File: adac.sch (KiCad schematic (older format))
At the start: 26 parts, among them J1 Conn_Coaxial, J2 Conn_Coaxial, J3 Conn_Coaxial, SW1 SW_SPST, U1 LTC1740, U2 TXS0108EPW, U3 TXS0108EPW, U4 AD7840

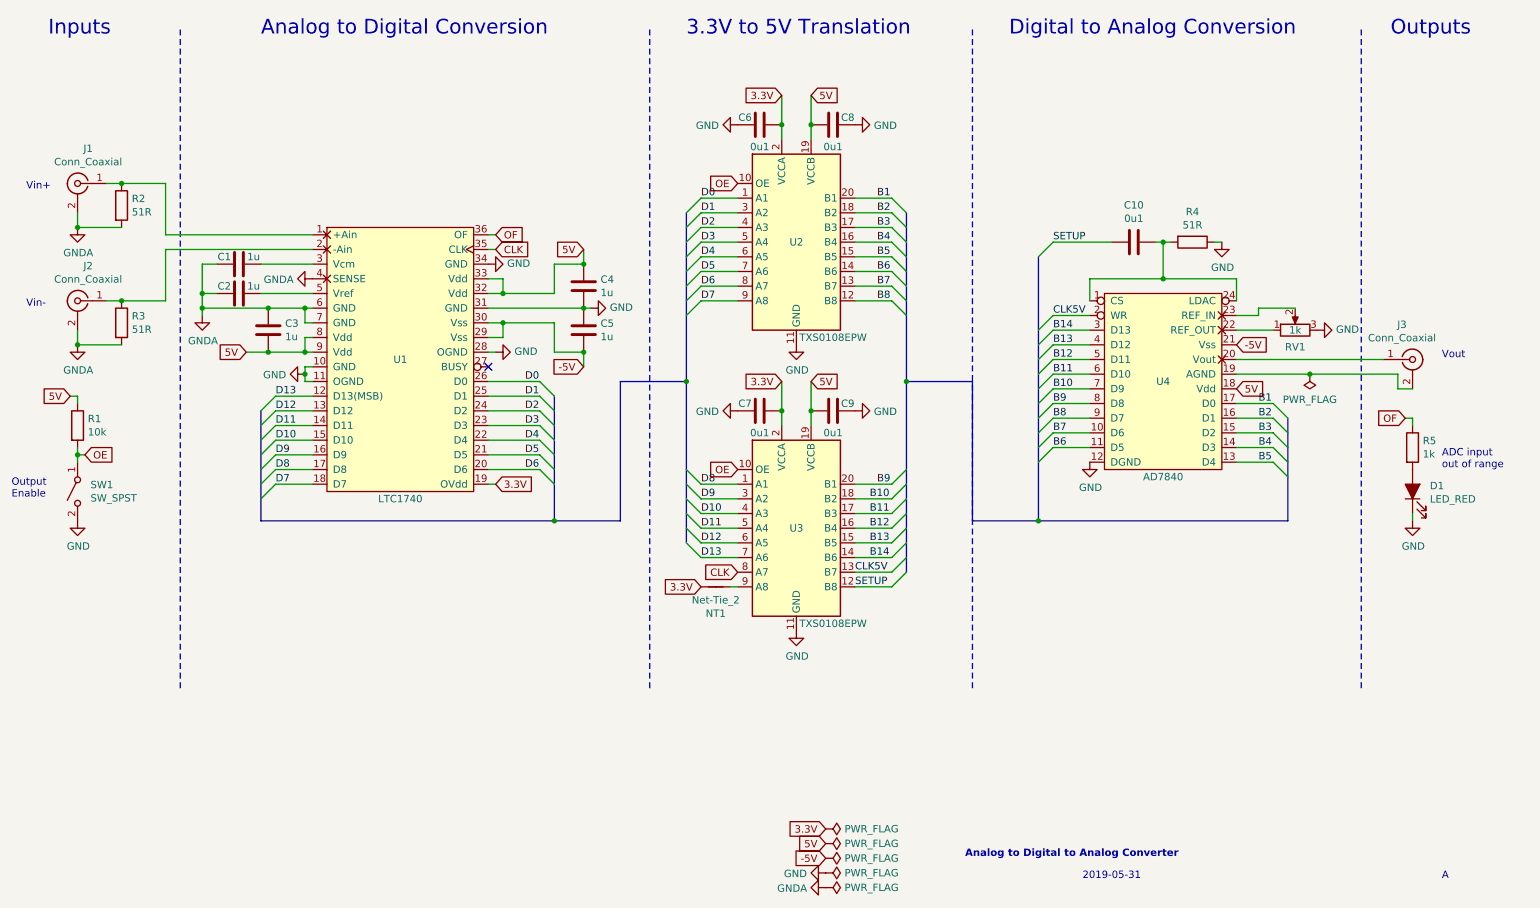
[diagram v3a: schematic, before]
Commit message: Add clock input connector
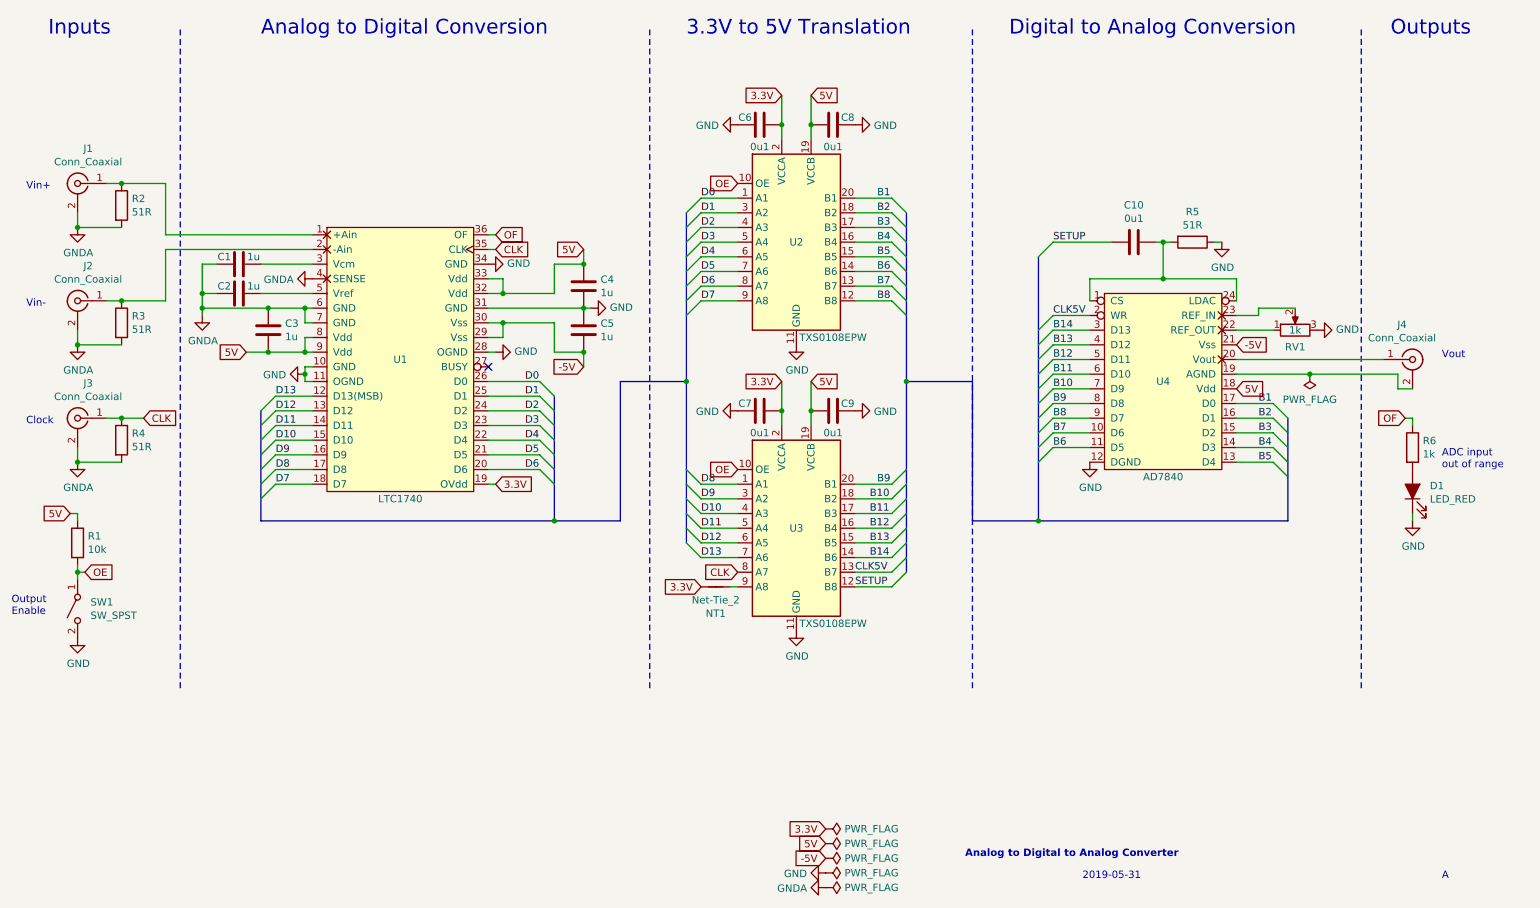
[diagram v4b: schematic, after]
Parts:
- added J3: Conn_Coaxial, Connector_Coaxial:BNC_TEConnectivity_1478204_Vertical, symbol Connector:Conn_Coaxial
- added R4: 51R, Resistor_THT:R_Axial_DIN0204_L3.6mm_D1.6mm_P7.62mm_Horizontal, symbol Device:R
- renumbered J3 to J4, R4 to R5, R5 to R6
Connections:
- net CLK: now also J3.1 (In), R4.1
- net GNDA: now also J3.2 (Ext), R4.2
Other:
- note added: "Clock"
- moved on the sheet: R1, SW1
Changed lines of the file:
@@
 	2850 4250 2850 4200
 $Comp
-L power:GND #PWR05
+L power:GND #PWR06
 U 1 1 5CF1A1D6
 P 2850 4200
-F 0 "#PWR05" H 2850 3950 50  0001 C CNN
+F 0 "#PWR06" H 2850 3950 50  0001 C CNN
 F 1 "GND" V 2855 4072 50  0000 R CNN
 F 2 "" H 2850 4200 50  0001 C CNN
@@
 	4150 3350 4100 3350
 $Comp
-L power:GND #PWR07
+L power:GND #PWR08
 U 1 1 5CF3FF9C
 P 4100 3450
-F 0 "#PWR07" H 4100 3200 50  0001 C CNN
+F 0 "#PWR08" H 4100 3200 50  0001 C CNN
 F 1 "GND" V 4105 3322 50  0000 R CNN
 F 2 "" H 4100 3450 50  0001 C CNN
@@
 Connection ~ 4200 3650
 $Comp
-L power:GND #PWR08
+L power:GND #PWR09
 U 1 1 5CF52655
 P 4150 4050
-F 0 "#PWR08" H 4150 3800 50  0001 C CNN
+F 0 "#PWR09" H 4150 3800 50  0001 C CNN
 F 1 "GND" V 4155 3922 50  0000 R CNN
 F 2 "" H 4150 4050 50  0001 C CNN
@@
 Connection ~ 4750 3450
 $Comp
-L power:GND #PWR012
+L power:GND #PWR013
 U 1 1 5CF89283
 P 6200 4000
-F 0 "#PWR012" H 6200 3750 50  0001 C CNN
+F 0 "#PWR013" H 6200 3750 50  0001 C CNN
 F 1 "GND" H 6205 3827 50  0000 C CNN
 F 2 "" H 6200 4000 50  0001 C CNN
@@
 5V
 $Comp
-L power:GND #PWR010
+L power:GND #PWR011
 U 1 1 5D00A6EA
 P 5800 2500
-F 0 "#PWR010" H 5800 2250 50  0001 C CNN
+F 0 "#PWR011" H 5800 2250 50  0001 C CNN
 F 1 "GND" V 5805 2372 50  0000 R CNN
 F 2 "" H 5800 2500 50  0001 C CNN
@@
 $EndComp
 $Comp
-L power:GND #PWR016
+L power:GND #PWR017
 U 1 1 5D0181CF
 P 6600 2500
-F 0 "#PWR016" H 6600 2250 50  0001 C CNN
+F 0 "#PWR017" H 6600 2250 50  0001 C CNN
 F 1 "GND" V 6605 2372 50  0000 R CNN
 F 2 "" H 6600 2500 50  0001 C CNN
@@
 	6300 2500 6300 2600
 $Comp
-L power:GND #PWR013
+L power:GND #PWR014
 U 1 1 5D02ED9B
 P 6200 5950
-F 0 "#PWR013" H 6200 5700 50  0001 C CNN
+F 0 "#PWR014" H 6200 5700 50  0001 C CNN
 F 1 "GND" H 6205 5777 50  0000 C CNN
 F 2 "" H 6200 5950 50  0001 C CNN
@@
 3.3V
 $Comp
-L power:GND #PWR011
+L power:GND #PWR012
 U 1 1 5D02EDC2
 P 5800 4450
-F 0 "#PWR011" H 5800 4200 50  0001 C CNN
+F 0 "#PWR012" H 5800 4200 50  0001 C CNN
 F 1 "GND" V 5805 4322 50  0000 R CNN
 F 2 "" H 5800 4450 50  0001 C CNN
@@
 $EndComp
 $Comp
-L power:GND #PWR017
+L power:GND #PWR018
 U 1 1 5D02EDD1
 P 6600 4450
-F 0 "#PWR017" H 6600 4200 50  0001 C CNN
+F 0 "#PWR018" H 6600 4200 50  0001 C CNN
 F 1 "GND" V 6605 4322 50  0000 R CNN
 F 2 "" H 6600 4450 50  0001 C CNN
@@
 	7400 4250 7400 5200
 $Comp
-L power:GND #PWR018
+L power:GND #PWR019
 U 1 1 5D1BFBF2
 P 8200 4800
-F 0 "#PWR018" H 8200 4550 50  0001 C CNN
+F 0 "#PWR019" H 8200 4550 50  0001 C CNN
 F 1 "GND" H 8205 4627 50  0000 C CNN
 F 2 "" H 8200 4800 50  0001 C CNN
@@
 -5V
 $Comp
-L Connector:Conn_Coaxial J3
+L Connector:Conn_Coaxial J4
 U 1 1 5D1CF67C
 P 10400 4100
-F 0 "J3" H 10328 4338 50  0000 C CNN
+F 0 "J4" H 10328 4338 50  0000 C CNN
 F 1 "Conn_Coaxial" H 10328 4247 50  0000 C CNN
 F 2 "Connector_Coaxial:BNC_TEConnectivity_1478204_Vertical" H 10400 4100 50  0001 C CNN
@@
 $EndComp
 $Comp
-L power:GND #PWR019
+L power:GND #PWR020
 U 1 1 5CFA5CCE
 P 9100 3300
-F 0 "#PWR019" H 9100 3050 50  0001 C CNN
+F 0 "#PWR020" H 9100 3050 50  0001 C CNN
 F 1 "GND" H 9105 3127 50  0000 C CNN
 F 2 "" H 9100 3300 50  0001 C CNN
@@
 	7950 3300 8350 3300
 $Comp
-L Device:R R4
+L Device:R R5
 U 1 1 5CFBE4B5
 P 8900 3300
-F 0 "R4" V 8693 3300 50  0000 C CNN
+F 0 "R5" V 8693 3300 50  0000 C CNN
 F 1 "51R" V 8784 3300 50  0000 C CNN
 F 2 "Resistor_THT:R_Axial_DIN0204_L3.6mm_D1.6mm_P7.62mm_Horizontal" V 8830 3300 50  0001 C CNN
@@
 $EndComp
 $Comp
-L power:GND #PWR020
+L power:GND #PWR021
 U 1 1 5D028740
 P 9750 3900
-F 0 "#PWR020" H 9750 3650 50  0001 C CNN
+F 0 "#PWR021" H 9750 3650 50  0001 C CNN
 F 1 "GND" V 9755 3772 50  0000 R CNN
 F 2 "" H 9750 3900 50  0001 C CNN
@@
 Text Notes 8150 7650 0    50   ~ 0
 2019-05-31
-Text GLabel 1350 4750 2    50   Input ~ 0
+Text GLabel 1350 5550 2    50   Input ~ 0
 OE
 $Comp
 L Device:R R1
 U 1 1 5D065464
-P 1300 4550
-F 0 "R1" H 1370 4596 50  0000 L CNN
-F 1 "10k" H 1370 4505 50  0000 L CNN
-F 2 "Resistor_THT:R_Axial_DIN0204_L3.6mm_D1.6mm_P7.62mm_Horizontal" V 1230 4550 50  0001 C CNN
-F 3 "~" H 1300 4550 50  0001 C CNN
-	1    1300 4550
-	1    0    0    -1
-$EndComp
-Text GLabel 1250 4350 0    50   Input ~ 0
+P 1300 5350
+F 0 "R1" H 1370 5396 50  0000 L CNN
+F 1 "10k" H 1370 5305 50  0000 L CNN
+F 2 "Resistor_THT:R_Axial_DIN0204_L3.6mm_D1.6mm_P7.62mm_Horizontal" V 1230 5350 50  0001 C CNN
+F 3 "~" H 1300 5350 50  0001 C CNN
+	1    1300 5350
+	1    0    0    -1
+$EndComp
+Text GLabel 1250 5150 0    50   Input ~ 0
 5V
 Wire Wire Line
-	1300 4750 1300 4700
-Connection ~ 1300 4750
-Wire Wire Line
-	1300 4750 1350 4750
-Wire Wire Line
-	1250 4350 1300 4350
-Wire Wire Line
-	1300 4350 1300 4400
+	1300 5550 1300 5500
+Connection ~ 1300 5550
+Wire Wire Line
+	1300 5550 1350 5550
+Wire Wire Line
+	1250 5150 1300 5150
+Wire Wire Line
+	1300 5150 1300 5200
 $Comp
 L Switch:SW_SPST SW1
 U 1 1 5D0D07C8
-P 1300 5000
-F 0 "SW1" V 1254 4912 50  0000 R CNN
-F 1 "SW_SPST" V 1345 4912 50  0000 R CNN
-F 2 "Button_Switch_THT:SW_CuK_JS202011CQN_DPDT_Straight" H 1300 5000 50  0001 C CNN
-F 3 "~" H 1300 5000 50  0001 C CNN
-	1    1300 5000
+P 1300 5800
+F 0 "SW1" V 1254 5712 50  0000 R CNN
+F 1 "SW_SPST" V 1345 5712 50  0000 R CNN
+F 2 "Button_Switch_THT:SW_CuK_JS202011CQN_DPDT_Straight" H 1300 5800 50  0001 C CNN
+F 3 "~" H 1300 5800 50  0001 C CNN
+	1    1300 5800
 	0    -1   1    0
 $EndComp
 Wire Wire Line
-	1300 4800 1300 4750
-$Comp
-L power:GND #PWR03
+	1300 5600 1300 5550
+$Comp
+L power:GND #PWR04
 U 1 1 5D0D88A4
-P 1300 5200
-F 0 "#PWR03" H 1300 4950 50  0001 C CNN
-F 1 "GND" H 1305 5027 50  0000 C CNN
-F 2 "" H 1300 5200 50  0001 C CNN
-F 3 "" H 1300 5200 50  0001 C CNN
-	1    1300 5200
+P 1300 6000
+F 0 "#PWR04" H 1300 5750 50  0001 C CNN
+F 1 "GND" H 1305 5827 50  0000 C CNN
+F 2 "" H 1300 6000 50  0001 C CNN
+F 3 "" H 1300 6000 50  0001 C CNN
+	1    1300 6000
 	1    0    0    -1
 $EndComp
@@
 Text Notes 950  3750 0    50   ~ 0
 Vin-
-Text Notes 850  5050 0    50   ~ 0
+Text Notes 850  5850 0    50   ~ 0
 Output\nEnable
 Text GLabel 4150 3250 2    50   Input ~ 0
@@
 	10050 1850 10050 6350
 $Comp
-L Device:R R5
+L Device:R R6
 U 1 1 5D1B5B21
 P 10400 4700
-F 0 "R5" H 10470 4746 50  0000 L CNN
+F 0 "R6" H 10470 4746 50  0000 L CNN
 F 1 "1k" H 10470 4655 50  0000 L CNN
 F 2 "Resistor_THT:R_Axial_DIN0204_L3.6mm_D1.6mm_P7.62mm_Horizontal" V 10330 4700 50  0001 C CNN
@@
 $EndComp
 $Comp
-L power:GND #PWR021
+L power:GND #PWR022
 U 1 1 5D1BDCD3
 P 10400 5200
-F 0 "#PWR021" H 10400 4950 50  0001 C CNN
+F 0 "#PWR022" H 10400 4950 50  0001 C CNN
 F 1 "GND" H 10405 5027 50  0000 C CNN
 F 2 "" H 10400 5200 50  0001 C CNN
@@
 ADC input\nout of range
 $Comp
-L power:GNDA #PWR06
+L power:GNDA #PWR07
 U 1 1 5D22C5FE
 P 2900 3550
-F 0 "#PWR06" H 2900 3300 50  0001 C CNN
+F 0 "#PWR07" H 2900 3300 50  0001 C CNN
 F 1 "GNDA" V 2905 3423 50  0000 R CNN
 F 2 "" H 2900 3550 50  0001 C CNN
@@
 $EndComp
 $Comp
-L power:GNDA #PWR04
+L power:GNDA #PWR05
 U 1 1 5D22CE94
 P 2150 3800
-F 0 "#PWR04" H 2150 3550 50  0001 C CNN
+F 0 "#PWR05" H 2150 3550 50  0001 C CNN
 F 1 "GNDA" H 2155 3627 50  0000 C CNN
 F 2 "" H 2150 3800 50  0001 C CNN
@@
 	9700 4200 10300 4200
 $Comp
-L power:GND #PWR09
+L power:GND #PWR010
 U 1 1 5CF5F6BA
 P 4800 3750
-F 0 "#PWR09" H 4800 3500 50  0001 C CNN
+F 0 "#PWR010" H 4800 3500 50  0001 C CNN
 F 1 "GND" V 4805 3622 50  0000 R CNN
 F 2 "" H 4800 3750 50  0001 C CNN
@@
 $EndComp
 $Comp
-L power:GNDA #PWR015
+L power:GNDA #PWR016
 U 1 1 5CF5ED2B
 P 6400 7700
-F 0 "#PWR015" H 6400 7450 50  0001 C CNN
+F 0 "#PWR016" H 6400 7450 50  0001 C CNN
 F 1 "GNDA" V 6405 7573 50  0000 R CNN
 F 2 "" H 6400 7700 50  0001 C CNN
@@
 $EndComp
 $Comp
-L power:GND #PWR014
+L power:GND #PWR015
 U 1 1 5CF5E2AE
 P 6400 7600
-F 0 "#PWR014" H 6400 7350 50  0001 C CNN
+F 0 "#PWR015" H 6400 7350 50  0001 C CNN
 F 1 "GND" V 6405 7472 50  0000 R CNN
 F 2 "" H 6400 7600 50  0001 C CNN
@@
 Text GLabel 5550 5650 0    50   Input ~ 0
 3.3V
+Connection ~ 1300 4800
+$Comp
+L power:GNDA #PWR03
+U 1 1 5CF2BD66
+P 1300 4800
+F 0 "#PWR03" H 1300 4550 50  0001 C CNN
+F 1 "GNDA" H 1305 4627 50  0000 C CNN
+F 2 "" H 1300 4800 50  0001 C CNN
+F 3 "" H 1300 4800 50  0001 C CNN
+	1    1300 4800
+	1    0    0    -1
+$EndComp
+Wire Wire Line
+	1500 4500 1600 4500
+Wire Wire Line
+	1300 4800 1600 4800
+Wire Wire Line
+	1300 4700 1300 4800
+$Comp
+L Connector:Conn_Coaxial J3
+U 1 1 5CF2BD6F
+P 1300 4500
+F 0 "J3" H 1228 4738 50  0000 C CNN
+F 1 "Conn_Coaxial" H 1228 4647 50  0000 C CNN
+F 2 "Connector_Coaxial:BNC_TEConnectivity_1478204_Vertical" H 1300 4500 50  0001 C CNN
+F 3 " ~" H 1300 4500 50  0001 C CNN
+	1    1300 4500
+	-1   0    0    -1
+$EndComp
+Text Notes 950  4550 0    50   ~ 0
+Clock
+Text GLabel 1750 4500 2    50   Input ~ 0
+CLK
+$Comp
+L Device:R R4
+U 1 1 5CF3ACE7
+P 1600 4650
+F 0 "R4" H 1670 4696 50  0000 L CNN
+F 1 "51R" H 1670 4605 50  0000 L CNN
+F 2 "Resistor_THT:R_Axial_DIN0204_L3.6mm_D1.6mm_P7.62mm_Horizontal" V 1530 4650 50  0001 C CNN
+F 3 "~" H 1600 4650 50  0001 C CNN
+	1    1600 4650
+	1    0    0    -1
+$EndComp
+Wire Wire Line
+	1600 4500 1750 4500
 Wire Bus Line
 	9550 4500 9550 5200
@@
 Wire Bus Line
 	5450 3100 5450 4250
+Connection ~ 1600 4500
 $EndSCHEMATC
